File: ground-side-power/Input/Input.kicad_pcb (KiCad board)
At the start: 2 copper layers, 36 parts, among them J1 Battery Terminals, J2 Battery Terminals, J27 Conn_01x02_Female, J3 Battery Terminals, J4 Battery Terminals, J5 455860005, J6 455860005, J7 ATX-24, J8 Conn_01x03_Female, J9 Conn_01x03_Female, K1 AZ2150-1A-12DEF, SW1 GRB234A2NABA1, U1 INA180, U2 INA180

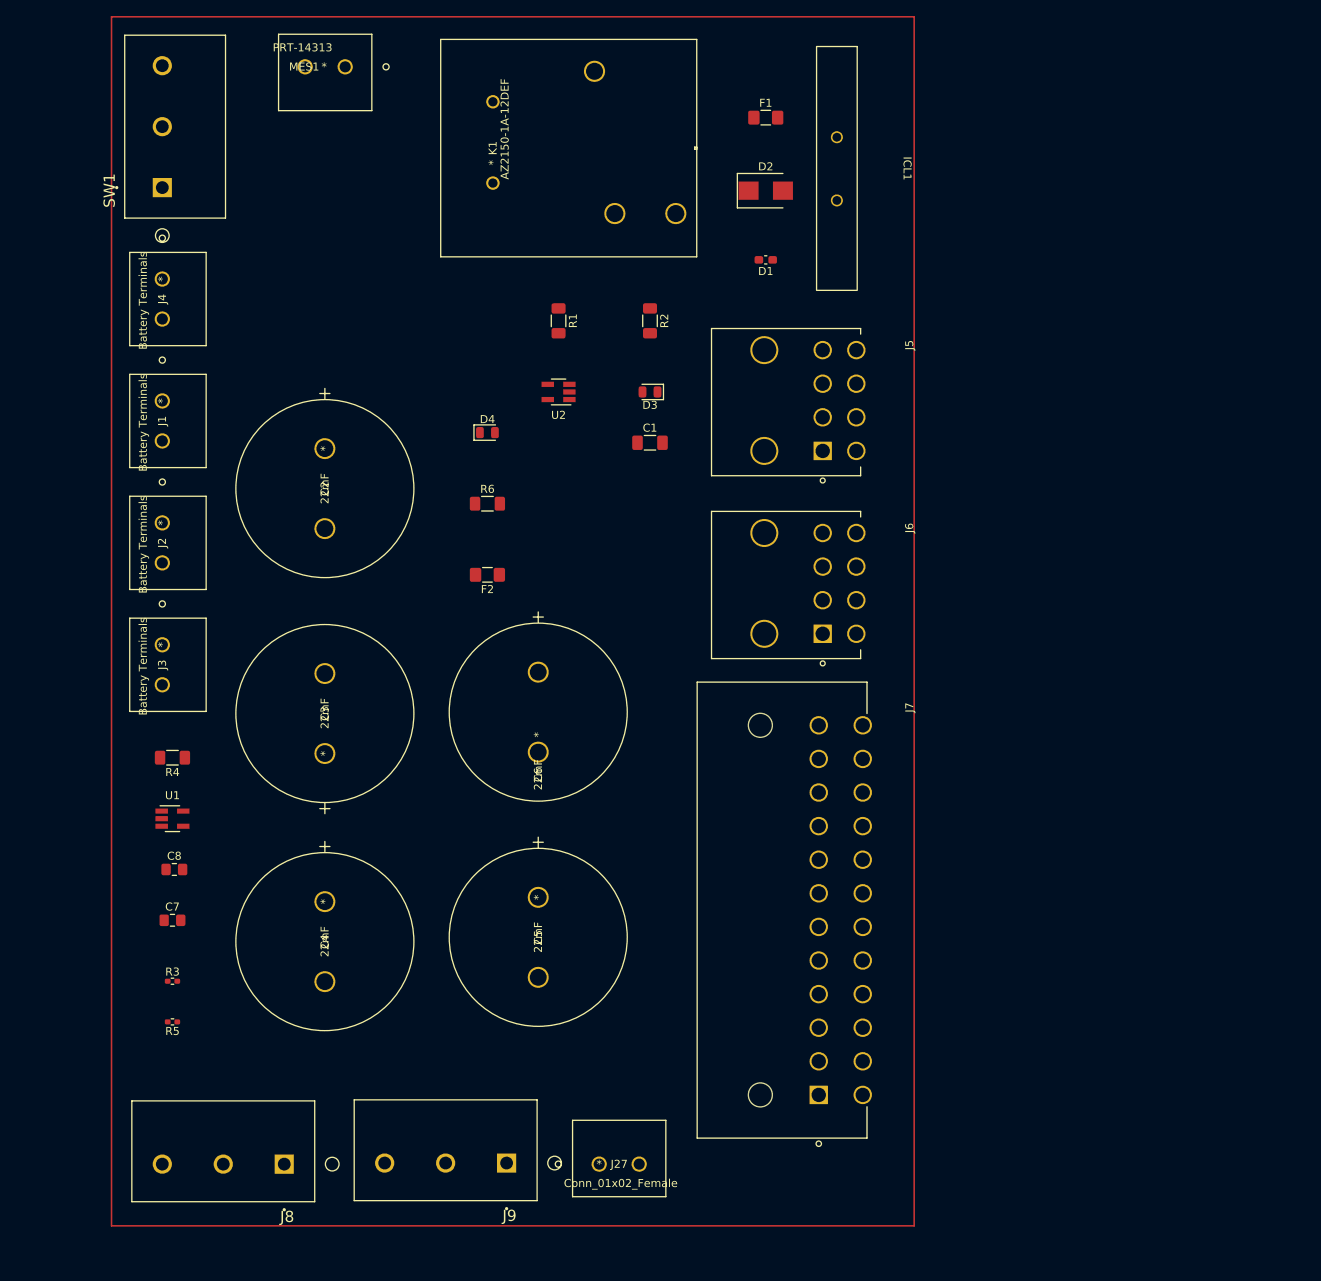
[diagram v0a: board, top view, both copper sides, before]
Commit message: Added Fan Headers + Thermistor
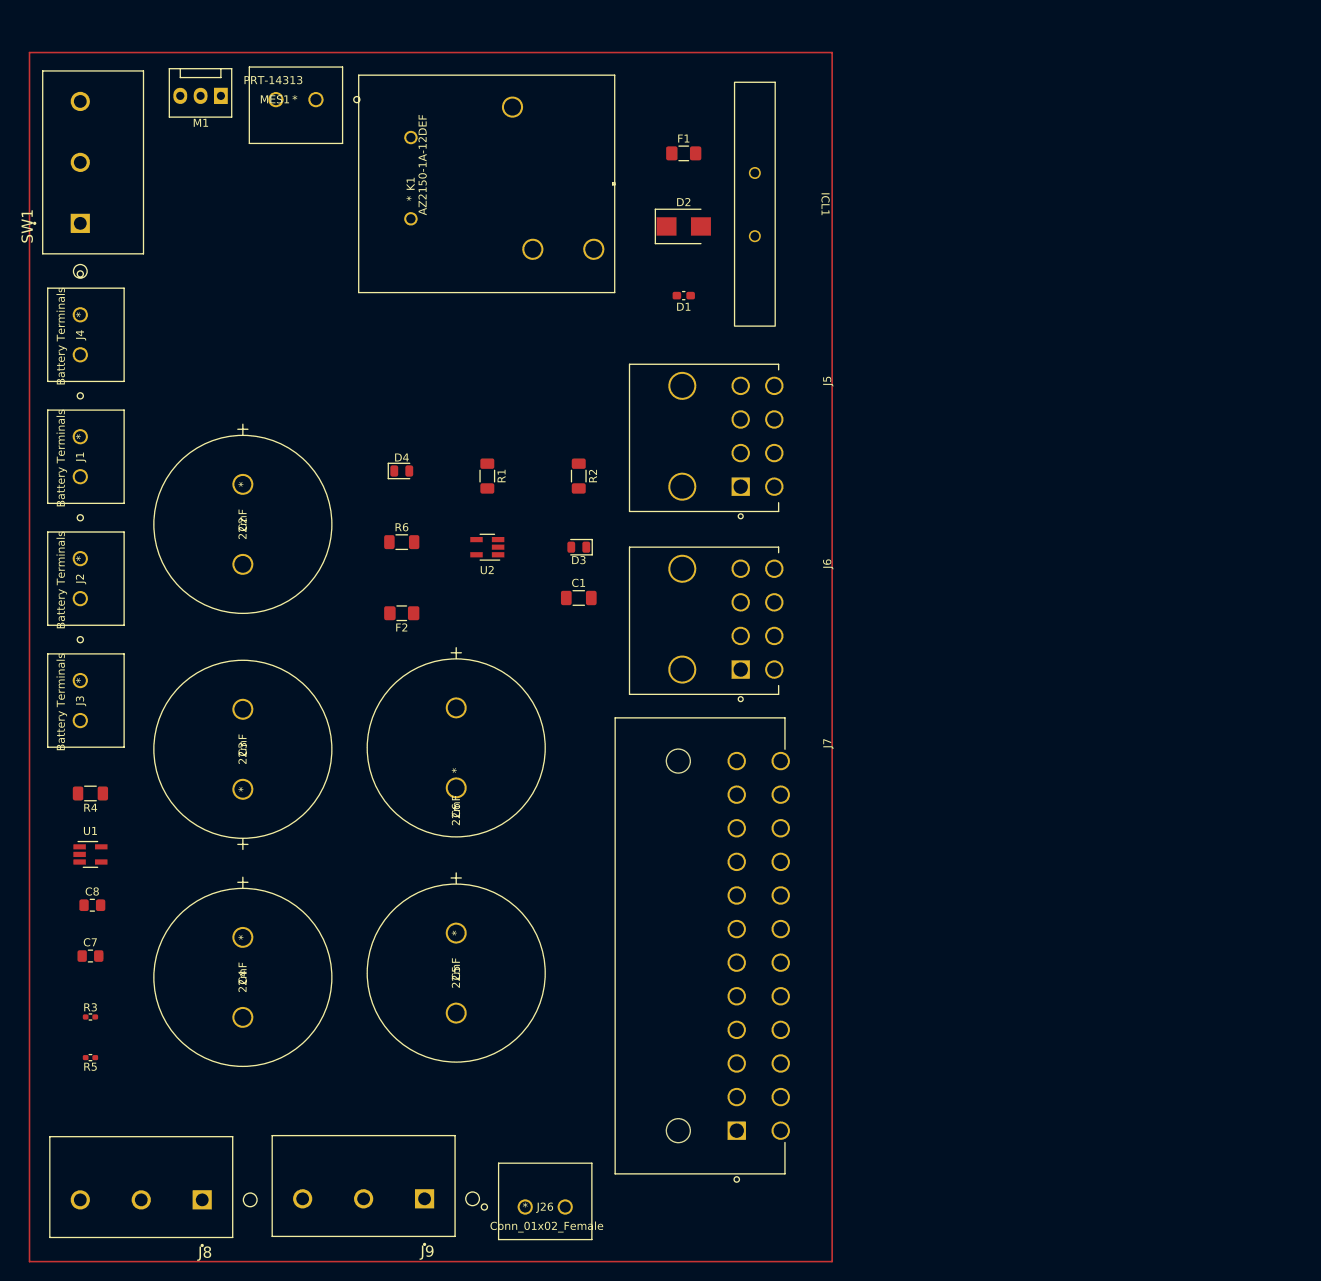
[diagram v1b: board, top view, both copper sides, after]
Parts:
- removed J27: Conn_01x02_Female, GSP:OSTTA020161
- added J26: Conn_01x02_Female, GSP:OSTTA020161, F.Cu at (102.5, 176.8)
- added M1: Fan_PC_Chassis, Connector:FanPinHeader_1x03_P2.54mm_Vertical, F.Cu at (64.5, 37.9)
- moved C1 21.4 mm to (109.2, 100.7)
- moved R1 21.4 mm to (97.8, 85.4)
- moved U2 21.4 mm to (97.8, 94.3)
- moved D3 21.4 mm to (109.2, 94.3)
- moved R2 21.4 mm to (109.2, 85.4)
- moved D4 11.7 mm to (87.1, 84.8)
- moved F2 11.7 mm to (87.1, 102.6)
- moved R6 11.7 mm to (87.1, 93.7)
- moved D1 11.2 mm to (122.3, 62.9)
- moved D2 11.2 mm to (122.3, 54.2)
- moved F1 11.2 mm to (122.3, 45.1)
- moved J7 11.2 mm to (129.0, 167.3)
- moved C3 11.2 mm to (67.2, 124.6)
- moved C4 11.2 mm to (67.2, 143.1)
- moved C5 11.2 mm to (93.9, 142.6)
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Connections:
- C1 pad 1: (no net) -> +BATT
- C1 pad 2: (no net) -> GND
- C2 pad 1: (no net) -> +12V
- C2 pad 2: (no net) -> GND
- C3 pad 1: (no net) -> +12V
- C3 pad 2: (no net) -> GND
- C4 pad 1: (no net) -> +12V
- C4 pad 2: (no net) -> GND
- C5 pad 1: (no net) -> +12V
- C5 pad 2: (no net) -> GND
- C6 pad 1: (no net) -> +12V
- C6 pad 2: (no net) -> GND
- C7 pad 1: (no net) -> GND
- C7 pad 2: (no net) -> +5V
- C8 pad 1: (no net) -> GND
- C8 pad 2: (no net) -> +5V
- D1 pad 1: (no net) -> Net-(D1-Pad1)
- D1 pad 2: (no net) -> GND
- D2 pad 1: (no net) -> Net-(D1-Pad1)
- D2 pad 2: (no net) -> Net-(D2-Pad2)
- D3 pad 1: (no net) -> Net-(D3-Pad1)
- D3 pad 2: (no net) -> +BATT
- D4 pad 1: (no net) -> Net-(D4-Pad1)
- D4 pad 2: (no net) -> +12V
- F1 pad 1: (no net) -> Net-(F1-Pad1)
- F1 pad 2: (no net) -> Net-(F1-Pad2)
- F2 pad 1: (no net) -> +BATT
- F2 pad 2: (no net) -> /12V_Sense+
- ICL1 pad 1: (no net) -> Net-(F1-Pad2)
- ICL1 pad 2: (no net) -> Net-(D2-Pad2)
- J1 pad 1: (no net) -> /BatteryPowerSupply
- J1 pad 2: (no net) -> GND
- J2 pad 1: (no net) -> /BatteryPowerSupply
- J2 pad 2: (no net) -> GND
- J3 pad 1: (no net) -> /BatteryPowerSupply
- J3 pad 2: (no net) -> GND
- J4 pad 1: (no net) -> /BatteryPowerSupply
- J4 pad 2: (no net) -> GND
- J5 pad 1: (no net) -> /ACPowerSupply
- J5 pad 2: (no net) -> /ACPowerSupply
- J5 pad 3: (no net) -> /ACPowerSupply
- J5 pad 4: (no net) -> GND
- J5 pad 5: (no net) -> GND
- J5 pad 6: (no net) -> GND
- J5 pad 7: (no net) -> GND
- J5 pad 8: (no net) -> GND
- J6 pad 1: (no net) -> /ACPowerSupply
- J6 pad 2: (no net) -> /ACPowerSupply
- J6 pad 3: (no net) -> /ACPowerSupply
- J6 pad 4: (no net) -> GND
- J6 pad 5: (no net) -> GND
- J6 pad 6: (no net) -> GND
- J6 pad 7: (no net) -> GND
- J6 pad 8: (no net) -> GND
- J7 pad 1: (no net) -> unconnected-(J7-Pad1)
- J7 pad 10: (no net) -> /ACPowerSupply
- J7 pad 11: (no net) -> /ACPowerSupply
- J7 pad 12: (no net) -> unconnected-(J7-Pad1)
- J7 pad 13: (no net) -> unconnected-(J7-Pad1)
- J7 pad 14: (no net) -> unconnected-(J7-Pad14)
- J7 pad 15: (no net) -> GND
- J7 pad 16: (no net) -> GND
- J7 pad 17: (no net) -> GND
- J7 pad 18: (no net) -> GND
- J7 pad 19: (no net) -> GND
- J7 pad 2: (no net) -> unconnected-(J7-Pad1)
- J7 pad 20: (no net) -> unconnected-(J7-Pad20)
- J7 pad 21: (no net) -> unconnected-(J7-Pad21)
- J7 pad 22: (no net) -> unconnected-(J7-Pad21)
- J7 pad 23: (no net) -> unconnected-(J7-Pad21)
- J7 pad 24: (no net) -> GND
- J7 pad 3: (no net) -> GND
- J7 pad 4: (no net) -> unconnected-(J7-Pad21)
- J7 pad 5: (no net) -> GND
- J7 pad 6: (no net) -> unconnected-(J7-Pad21)
- J7 pad 7: (no net) -> GND
- J7 pad 8: (no net) -> unconnected-(J7-Pad8)
- J7 pad 9: (no net) -> unconnected-(J7-Pad9)
- J8 pad 1: (no net) -> +12V
- J8 pad 2: (no net) -> +BATT
- J8 pad 3: (no net) -> GND
- J9 pad 1: (no net) -> /12V_OUT
- J9 pad 2: (no net) -> /TOTAL_OUT
- J9 pad 3: (no net) -> /12_VOLTAGE
- K1 pad 1: (no net) -> GND
- K1 pad 2: (no net) -> /Sys_Sense+
- K1 pad 3: (no net) -> unconnected-(K1-Pad3)
- K1 pad 4: (no net) -> Net-(D2-Pad2)
- K1 pad 5: (no net) -> Net-(D1-Pad1)
- MES1 pad 1: (no net) -> GND
- MES1 pad 2: (no net) -> +BATT
- R1 pad 1: (no net) -> /Sys_Sense+
- R1 pad 2: (no net) -> +BATT
- R2 pad 1: (no net) -> GND
- R2 pad 2: (no net) -> Net-(D3-Pad1)
- R3 pad 1: (no net) -> +12V
- R3 pad 2: (no net) -> /12_VOLTAGE
- R4 pad 1: (no net) -> /12V_Sense+
- R4 pad 2: (no net) -> +12V
- R5 pad 1: (no net) -> /12_VOLTAGE
- R5 pad 2: (no net) -> GND
- R6 pad 1: (no net) -> GND
- R6 pad 2: (no net) -> Net-(D4-Pad1)
- SW1 pad 1: (no net) -> /ACPowerSupply
- SW1 pad 2: (no net) -> Net-(F1-Pad1)
- SW1 pad 3: (no net) -> /BatteryPowerSupply
- U1 pad 1: (no net) -> /12V_OUT
- U1 pad 2: (no net) -> GND
- U1 pad 3: (no net) -> /12V_Sense+
- U1 pad 4: (no net) -> +12V
- U1 pad 5: (no net) -> +5V
- U2 pad 1: (no net) -> /TOTAL_OUT
- U2 pad 2: (no net) -> GND
- U2 pad 3: (no net) -> /Sys_Sense+
- U2 pad 4: (no net) -> +BATT
- U2 pad 5: (no net) -> +5V

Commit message: PCB Layout First Draft
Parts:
- added ?: , clipboard:ee0da358-bf61-46f9-af96-80582bde7c0f, F.Cu at (44.7, 36.5)
- added ?: , , F.Cu at (45.2, 158.0)
- added ?: , , F.Cu at (136.4, 158.2)
- added ?: , , F.Cu at (136.7, 36.8)
- C1, C8, D1, D2, F1, F2, R1, R4, U2: moved to B.Cu
- K1: value AZ2150-1A-12DEF -> AZ2150_AMZ
- moved C8 83.5 mm to (94.7, 69.6)
- moved MES1 79.1 mm to (47.6, 112.1), turned to -90 degrees
- moved R2 73.3 mm to (47.0, 124.2), turned to 0 degrees
- moved C7 68.3 mm to (85.3, 88.1), turned to 90 degrees
- moved M1 63.9 mm to (47.5, 99.6), turned to -90 degrees
- moved D3 63.1 mm to (53.6, 124.2), turned to 0 degrees
- moved U1 63.1 mm to (91.7, 87.1), turned to 180 degrees
- moved R4 58.7 mm to (94.7, 89.4), turned to -90 degrees
- moved C4 57.6 mm to (98.8, 95.0)
- moved D4 55.3 mm to (53.6, 128.8)
- moved R6 53.3 mm to (47.0, 128.8)
- moved SW1 52.2 mm to (98.0, 43.5), turned to 180 degrees
- moved J8 40.4 mm to (93.7, 150.7), turned to 0 degrees
- moved R3 39.9 mm to (86.9, 143.5), turned to 180 degrees
- moved J3 39.5 mm to (47.8, 71.5)
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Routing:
- net +BATT: track 0.00 -> 166.0 mm
- net /12V_OUT: track 0.00 -> 140.3 mm, vias 0 -> 1
- net /TOTAL_OUT: track 0.00 -> 139.1 mm
- net +5V: track 0.00 -> 129.3 mm, vias 0 -> 1
- net +12V: track 0.00 -> 77.3 mm
- net GND: track 0.00 -> 30.2 mm
- net /12_VOLTAGE: track 0.00 -> 10.1 mm
- net /Sys_Sense+: track 0.00 -> 9.33 mm
- net Net-(D2-Pad2): track 0.00 -> 8.46 mm
- net Net-(D1-Pad1): track 0.00 -> 7.82 mm
- net Net-(D4-Pad1): track 0.00 -> 4.12 mm
- net Net-(D3-Pad1): track 0.00 -> 4.12 mm
- net /12V_Sense+: track 0.00 -> 3.76 mm, vias 0 -> 1
- added copper zone on B.Cu, net +12V
- added copper zone on B.Cu, net +BATT
- added copper zone on B.Cu, net /12V_Sense+
- added copper zone on B.Cu, net /ACPowerSupply
- added copper zone on B.Cu, net /BatteryPowerSupply
- added copper zone on B.Cu, net /Sys_Sense+
- added copper zone on F.Cu, net GND
- added copper zone on B.Cu, net Net-(D2-Pad2)
- added copper zone on B.Cu, net Net-(F1-Pad1)
- added copper zone on B.Cu, net Net-(F1-Pad2)
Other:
- board outline added: 100.3 x 130 mm
- board text added: "+"
- board text added: "+12"
- board text added: "+12 Current"
- board text added: "+12 Voltage"
- board text added: "+5"
- board text added: "+BATT"
- board text added: "-"
- board text added: "0"
- board text added: "AC"
- board text added: "DC"
- board text added: "Don't Populate"
- board text added: "SWITCH"
- board text added: "Total Current"
